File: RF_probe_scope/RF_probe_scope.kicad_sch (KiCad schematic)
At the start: 34 parts, among them J1 INPUT, Q1 BFR92, Q2 BFR92, Q3 BFT92, Q4 BFT92, Q5 BFR92, Q6 BFT92, SW1 SW_SPST

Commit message: Added virtual ground circuit
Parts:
- added C10, C11, C12: 10u, symbol Device:C
- added C9: 100p, symbol Device:C
- added J2: Conn_Coaxial, symbol Connector:Conn_Coaxial
- added J3: INPUT -, symbol Connector_Generic:Conn_01x01
- added L5: 22u, symbol Device:L_Iron
- added R15, R16: 10k, symbol Device:R
- added U1: TL071, symbol Amplifier_Operational:TL071
- J1: value INPUT -> INPUT +
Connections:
- net -12V: now also L3.2, C11.2, J2.2 (Ext), R16.2, U1.4 (V-)
- net GND: now also C10.2, C11.1, C12.2, C9.2, J3.1 (Pin_1), U1.2 (-), U1.6
- net +24V: now reaches L4.2
- net +24V: now also C10.1, C12.1, C9.1, L5.1, R15.1, U1.7 (V+)
- net at C4.2: now also J2.1 (In), L5.2
- new net: R15.2, R16.1, U1.3 (+)
- no-connect marks 0 -> 2
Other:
- moved on the sheet: C1, C2, C3, C4, C5, C6, C7, C8, J1, L1, L2, L3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

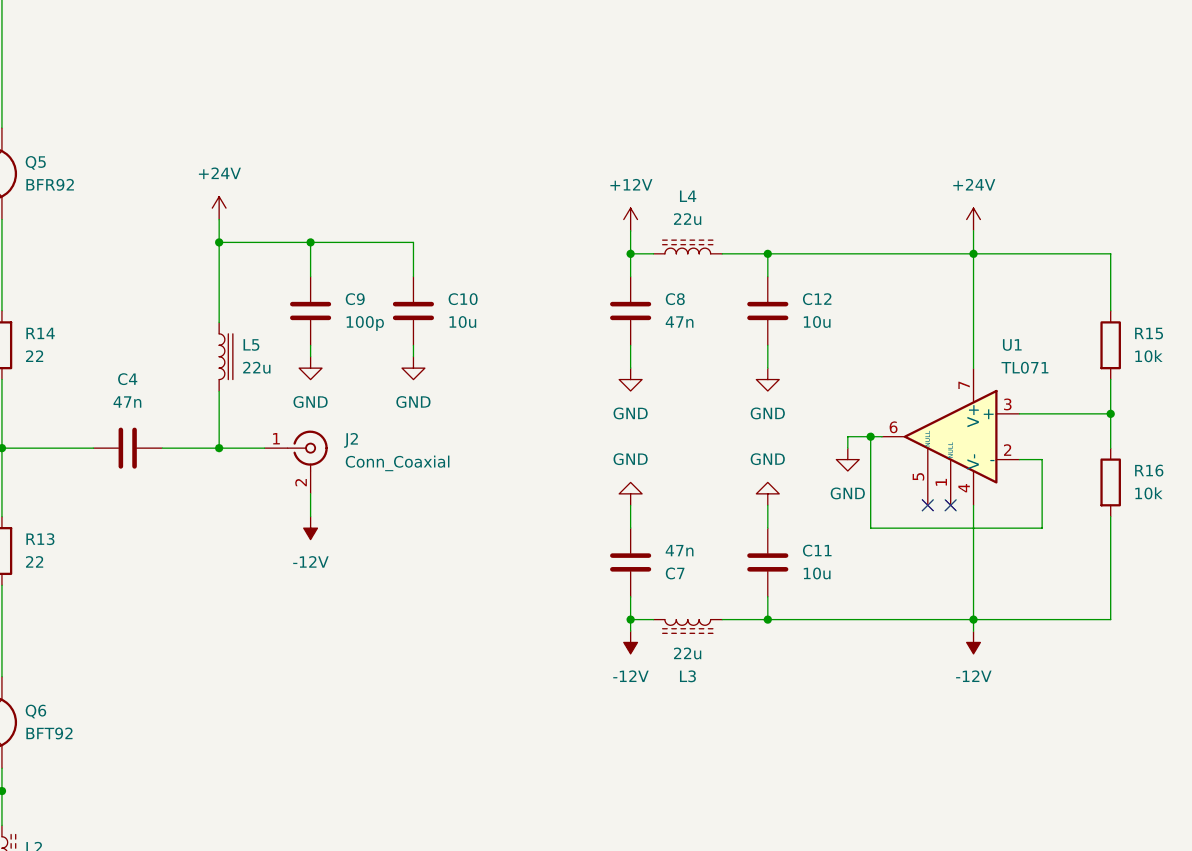
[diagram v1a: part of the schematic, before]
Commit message: Restored symmetrical power supply
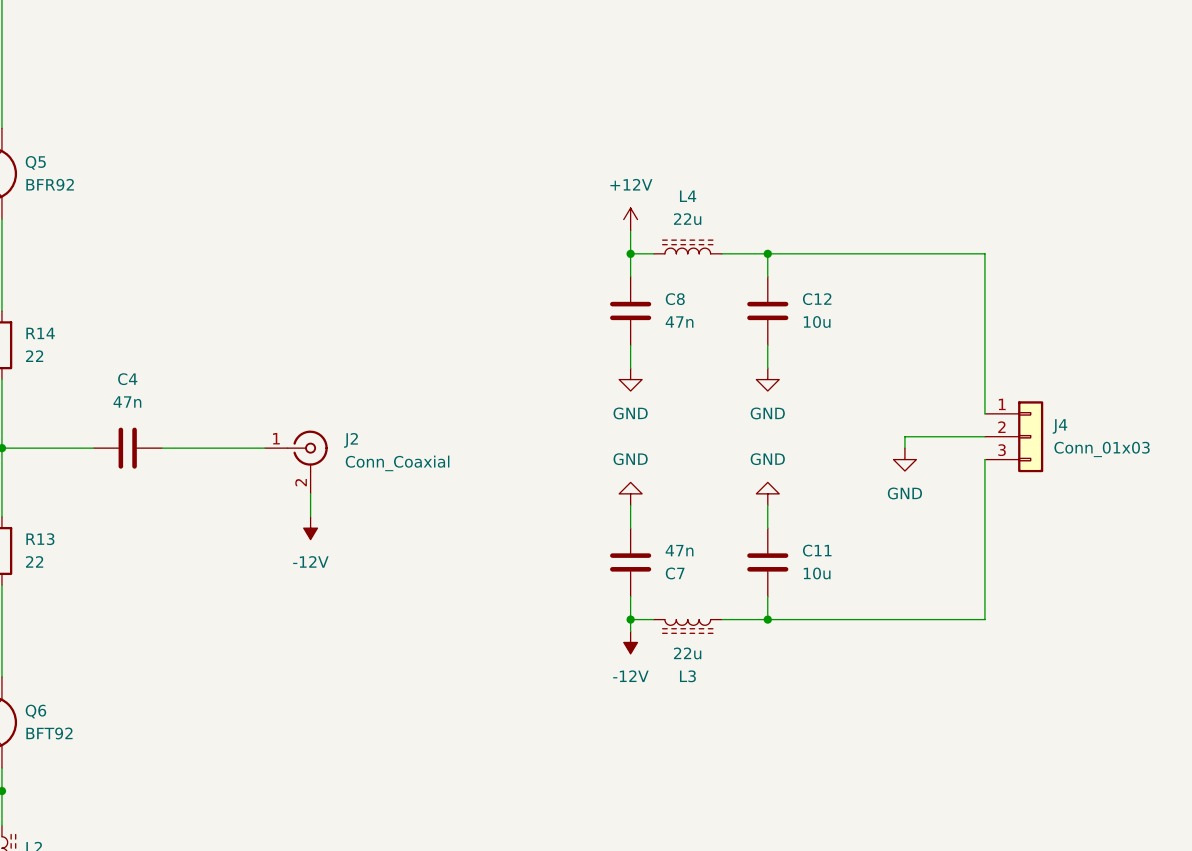
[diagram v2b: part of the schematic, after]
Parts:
- removed C10: 10u, symbol Device:C
- removed C9: 100p, symbol Device:C
- removed L5: 22u, symbol Device:L_Iron
- removed R15, R16: 10k, symbol Device:R
- removed U1: TL071, symbol Amplifier_Operational:TL071
- added J4: Conn_01x03, symbol Connector_Generic:Conn_01x03
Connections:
- net -12V: no longer C11.2, L3.2
- net GND: now also J4.2 (Pin_2)
- net +24V: no longer names the net of C12.1, L4.2
- net +24V: now also J4.1 (Pin_1)
- new net: C11.2, J4.3 (Pin_3), L3.2
- no-connect marks 2 -> 0

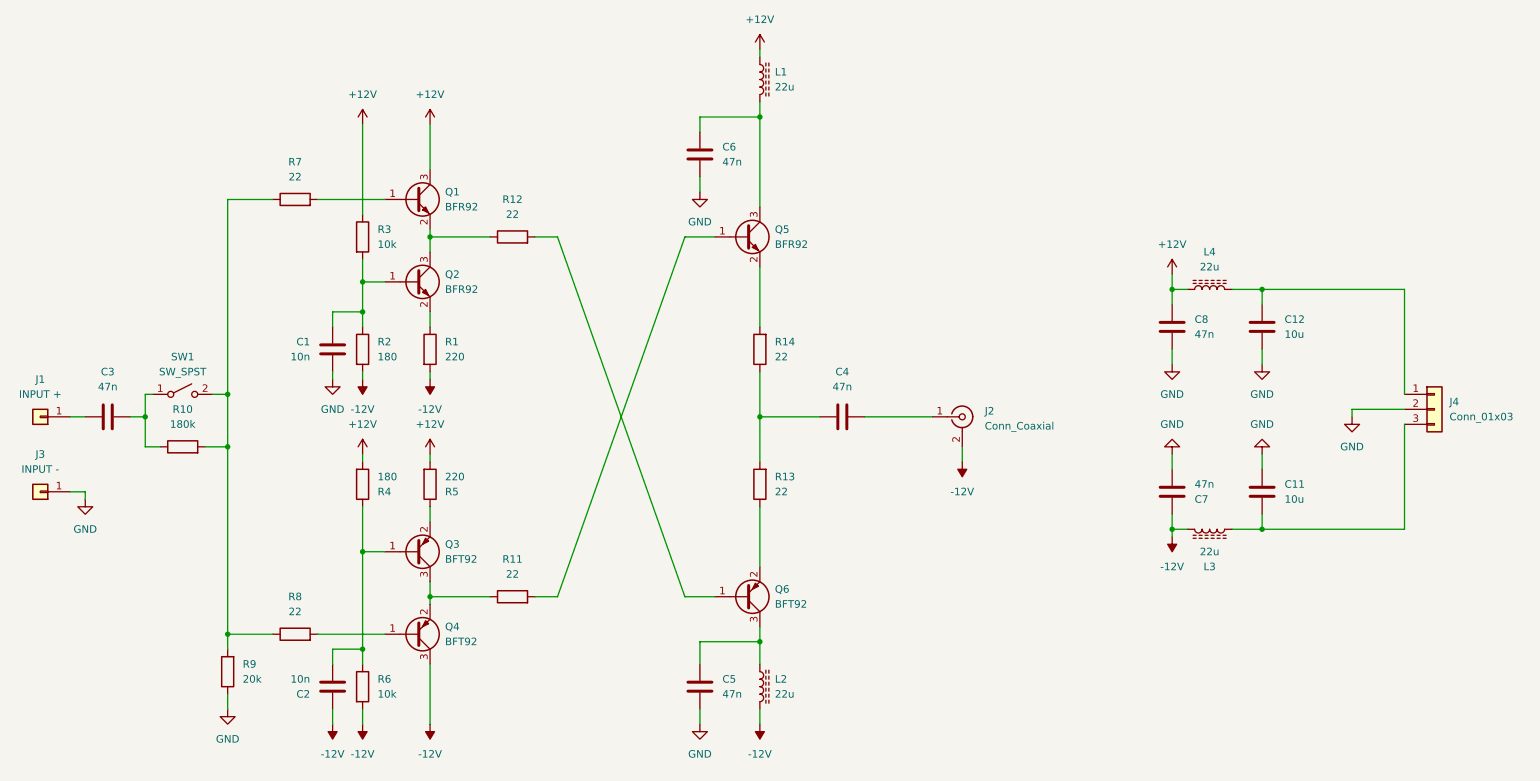
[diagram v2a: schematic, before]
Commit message: First non-symmetrical version
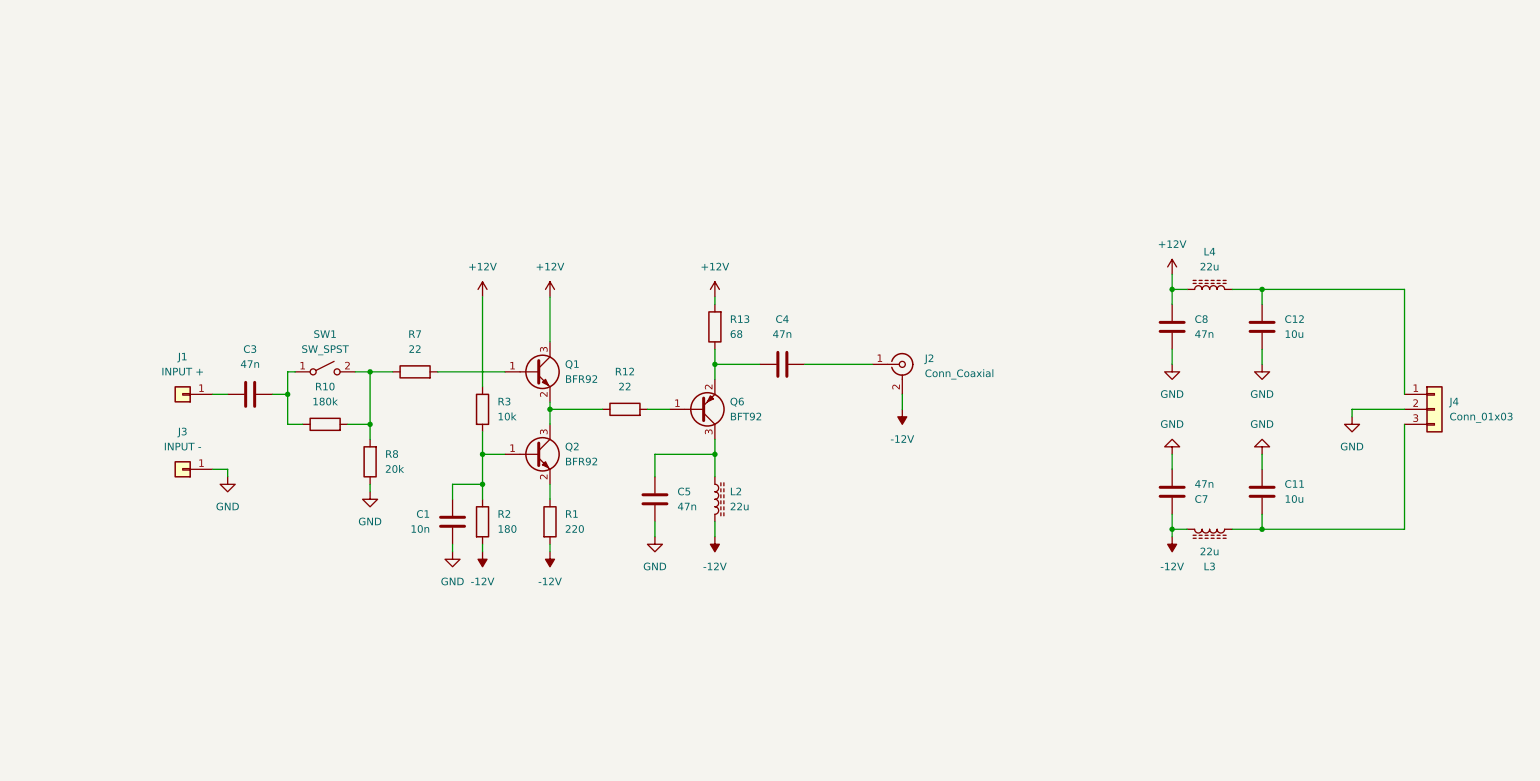
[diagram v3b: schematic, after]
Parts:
- removed C2: 10n, symbol Device:C
- removed C6: 47n, symbol Device:C
- removed L1: 22u, symbol Device:L_Ferrite
- removed Q3, Q4: BFT92, Package_TO_SOT_SMD:SOT-23, symbol Transistor_BJT:BFT92
- removed Q5: BFR92, Package_TO_SOT_SMD:SOT-323_SC-70, symbol Transistor_BJT:BFR92
- removed R11, R14: 22, symbol Device:R
- removed R4: 180, symbol Device:R
- removed R5: 220, symbol Device:R
- removed R6: 10k, symbol Device:R
- removed R9: 20k, symbol Device:R
- R13: value 22 -> 68
- R8: value 22 -> 20k
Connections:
- net +12V: now also R13.2
- net GND: now also R8.1
- net at Q6.2 (E), R13.1: now also C4.1
- net at R10.2, R7.1, SW1.2 (B): now also R8.2; no longer R8.1
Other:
- moved on the sheet: C1, C3, C4, C5, J1, J2, J3, L2, Q1, Q2, Q6, R1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
